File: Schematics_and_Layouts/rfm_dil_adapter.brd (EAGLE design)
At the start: 31.8 x 22.9 mm, 17 parts

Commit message: Added Gerber Files
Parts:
- renumbered CLK to IO5, DCLK to IO1, FSK to IO2, GND1 to AGND, NINT to IO3, NIRQ to IO0, NRES to RES, NSEL to NSS, SDI to MOSI, SDO to MISO
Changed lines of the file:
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@@
 <?xml version="1.0" encoding="utf-8"?>
 <!DOCTYPE eagle SYSTEM "eagle.dtd">
-<eagle version="6.3">
+<eagle version="6.6.0">
 <drawing>
 <settings>
@@
 <setting verticaltext="up"/>
 </settings>
-<grid distance="1.27" unitdist="mm" unit="mm" style="lines" multiple="1" display="yes" altdistance="25" altunitdist="mil" altunit="mil"/>
+<grid distance="1.27" unitdist="mm" unit="mm" style="lines" multiple="1" display="yes" altdistance="12.5" altunitdist="mil" altunit="mil"/>
 <layers>
 <layer number="1" name="Top" color="4" fill="1" visible="yes" active="yes"/>
@@
 </autorouter>
 <elements>
-<element name="U$1" library="fp" package="RFM12_Z" value="RFM12_Z" x="15.24" y="12.7" rot="R270"/>
-<element name="CLK" library="solpad" package="SE13" value="SE13" x="2.54" y="10.16" rot="R270"/>
-<element name="DCLK" library="solpad" package="SE13" value="SE13" x="2.54" y="12.7" rot="R270"/>
-<element name="FSK" library="solpad" package="SE13" value="SE13" x="2.54" y="15.24" rot="R270"/>
-<element name="SDI" library="solpad" package="SE13" value="SE13" x="27.94" y="15.24" rot="R270"/>
-<element name="SDO" library="solpad" package="SE13" value="SE13" x="2.54" y="20.32" rot="R270"/>
-<element name="SCK" library="solpad" package="SE13" value="SE13" x="27.94" y="17.78" rot="R270"/>
-<element name="NSEL" library="solpad" package="SE13" value="SE13" x="27.94" y="20.32" rot="R270"/>
-<element name="GND" library="solpad" package="SE13" value="SE13" x="2.54" y="5.08" rot="R270"/>
-<element name="GND1" library="solpad" package="SE13" value="SE13" x="27.94" y="10.16" rot="R270"/>
-<element name="NRES" library="solpad" package="SE13" value="SE13" x="2.54" y="7.62" rot="R270"/>
-<element name="NIRQ" library="solpad" package="SE13" value="SE13" x="2.54" y="17.78" rot="R270"/>
-<element name="NINT" library="solpad" package="SE13" value="SE13" x="27.94" y="12.7" rot="R270"/>
-<element name="VDD" library="solpad" package="SE13" value="SE13" x="27.94" y="7.62" rot="R270"/>
-<element name="ANT+" library="testpad" package="TP20SQ" value="PTR1TP20SQ" x="22.885" y="2.54">
-<attribute name="TP_SIGNAL_NAME" value="" x="22.885" y="2.54" size="1.778" layer="27" display="off"/>
-</element>
-<element name="ANT_GND" library="testpad" package="TP20SQ" value="PTR1TP20SQ" x="18.635" y="2.54">
-<attribute name="TP_SIGNAL_NAME" value="" x="18.635" y="2.54" size="1.778" layer="27" display="off"/>
-</element>
-<element name="ANT_GND2" library="testpad" package="TP20SQ" value="PTR1TP20SQ" x="27.135" y="2.54">
-<attribute name="TP_SIGNAL_NAME" value="" x="27.135" y="2.54" size="1.778" layer="27" display="off"/>
+<element name="U$1" library="fp" package="RFM12_Z" value="RFM12_Z" x="15.24" y="12.7" smashed="yes" rot="R270"/>
+<element name="IO5" library="solpad" package="SE13" value="SE13" x="2.54" y="10.16" smashed="yes" rot="R270">
+<attribute name="NAME" x="4.191" y="11.43" size="0.8" layer="25" font="vector" ratio="20" rot="R270"/>
+</element>
+<element name="IO1" library="solpad" package="SE13" value="SE13" x="2.54" y="12.7" smashed="yes" rot="R270">
+<attribute name="NAME" x="4.191" y="13.97" size="0.8" layer="25" font="vector" ratio="20" rot="R270"/>
+</element>
+<element name="IO2" library="solpad" package="SE13" value="SE13" x="2.54" y="15.24" smashed="yes" rot="R270">
+<attribute name="NAME" x="4.191" y="16.51" size="0.8" layer="25" font="vector" ratio="20" rot="R270"/>
+</element>
+<element name="MOSI" library="solpad" package="SE13" value="SE13" x="27.94" y="15.24" smashed="yes" rot="R270">
+<attribute name="NAME" x="29.591" y="16.51" size="0.8" layer="25" font="vector" ratio="20" rot="R270"/>
+</element>
+<element name="MISO" library="solpad" package="SE13" value="SE13" x="2.54" y="20.32" smashed="yes" rot="R270">
+<attribute name="NAME" x="4.191" y="21.9075" size="0.8" layer="25" font="vector" ratio="20" rot="R270"/>
+</element>
+<element name="SCK" library="solpad" package="SE13" value="SE13" x="27.94" y="17.78" smashed="yes" rot="R270">
+<attribute name="NAME" x="29.591" y="19.05" size="0.8" layer="25" font="vector" ratio="20" rot="R270"/>
+</element>
+<element name="NSS" library="solpad" package="SE13" value="SE13" x="27.94" y="20.32" smashed="yes" rot="R270">
+<attribute name="NAME" x="29.591" y="21.59" size="0.8" layer="25" font="vector" ratio="20" rot="R270"/>
+</element>
+<element name="GND" library="solpad" package="SE13" value="SE13" x="2.54" y="5.08" smashed="yes" rot="R270">
+<attribute name="NAME" x="5.0165" y="3.81" size="0.8" layer="25" font="vector" ratio="20" rot="R90"/>
+</element>
+<element name="AGND" library="solpad" package="SE13" value="SE13" x="27.94" y="10.16" smashed="yes" rot="R270">
+<attribute name="NAME" x="29.591" y="11.7475" size="0.8" layer="25" font="vector" ratio="20" rot="R270"/>
+</element>
+<element name="RES" library="solpad" package="SE13" value="SE13" x="2.54" y="7.62" smashed="yes" rot="R270">
+<attribute name="NAME" x="4.191" y="8.89" size="0.8" layer="25" font="vector" ratio="20" rot="R270"/>
+</element>
+<element name="IO0" library="solpad" package="SE13" value="SE13" x="2.54" y="17.78" smashed="yes" rot="R270">
+<attribute name="NAME" x="4.191" y="19.05" size="0.8" layer="25" font="vector" ratio="20" rot="R270"/>
+</element>
+<element name="IO3" library="solpad" package="SE13" value="SE13" x="27.94" y="12.7" smashed="yes" rot="R270">
+<attribute name="NAME" x="29.591" y="13.6525" size="0.8" layer="25" font="vector" ratio="20" rot="R270"/>
+</element>
+<element name="VDD" library="solpad" package="SE13" value="SE13" x="27.94" y="7.62" smashed="yes" rot="R270">
+<attribute name="NAME" x="29.591" y="8.5725" size="0.8" layer="25" font="vector" ratio="20" rot="R270"/>
+</element>
+<element name="ANT+" library="testpad" package="TP20SQ" value="PTR1TP20SQ" x="22.885" y="2.54" smashed="yes">
+<attribute name="TP_SIGNAL_NAME" value="" x="22.885" y="0" size="1" layer="37"/>
+</element>
+<element name="ANT_GND" library="testpad" package="TP20SQ" value="PTR1TP20SQ" x="18.635" y="2.54" smashed="yes">
+<attribute name="TP_SIGNAL_NAME" value="" x="18.635" y="0" size="1" layer="37"/>
+</element>
+<element name="ANT_GND2" library="testpad" package="TP20SQ" value="PTR1TP20SQ" x="27.135" y="2.54" smashed="yes">
+<attribute name="TP_SIGNAL_NAME" value="" x="27.135" y="0" size="1" layer="37"/>
 </element>
 </elements>
@@
 <signal name="N$1">
 <contactref element="U$1" pad="CLK"/>
-<contactref element="CLK" pad="MP"/>
+<contactref element="IO5" pad="MP"/>
 <wire x1="2.54" y1="10.16" x2="3.08" y2="10.7" width="0.8128" layer="1"/>
 <wire x1="3.08" y1="10.7" x2="7.24" y2="10.7" width="0.8128" layer="1"/>
@@
 <signal name="N$2">
 <contactref element="U$1" pad="DCLK"/>
-<contactref element="DCLK" pad="MP"/>
+<contactref element="IO1" pad="MP"/>
 <wire x1="2.54" y1="12.7" x2="7.24" y2="12.7" width="0.8128" layer="1"/>
 </signal>
 <signal name="N$3">
 <contactref element="U$1" pad="FSK"/>
-<contactref element="FSK" pad="MP"/>
+<contactref element="IO2" pad="MP"/>
 <wire x1="2.54" y1="15.24" x2="3.08" y2="14.7" width="0.8128" layer="1"/>
 <wire x1="3.08" y1="14.7" x2="7.24" y2="14.7" width="0.8128" layer="1"/>
@@
 <signal name="N$4">
 <contactref element="U$1" pad="SDI"/>
-<contactref element="SDI" pad="MP"/>
+<contactref element="MOSI" pad="MP"/>
 <wire x1="27.94" y1="15.24" x2="27.4" y2="14.7" width="0.8128" layer="1"/>
 <wire x1="27.4" y1="14.7" x2="23.240003125" y2="14.7" width="0.8128" layer="1"/>
@@
 <signal name="N$5">
 <contactref element="U$1" pad="SDO"/>
-<contactref element="SDO" pad="MP"/>
+<contactref element="MISO" pad="MP"/>
 <wire x1="2.54" y1="20.32" x2="5.62" y2="20.32" width="0.8128" layer="1"/>
 <wire x1="5.62" y1="20.32" x2="7.239996875" y2="18.700003125" width="0.8128" layer="1"/>
@@
 <signal name="N$7">
 <contactref element="U$1" pad="NSEL"/>
-<contactref element="NSEL" pad="MP"/>
+<contactref element="NSS" pad="MP"/>
 <wire x1="27.94" y1="20.32" x2="24.86" y2="20.32" width="0.8128" layer="1"/>
 <wire x1="24.86" y1="20.32" x2="23.24" y2="18.7" width="0.8128" layer="1"/>
@@
 <signal name="N$11">
 <contactref element="U$1" pad="NRES"/>
-<contactref element="NRES" pad="MP"/>
+<contactref element="RES" pad="MP"/>
 <wire x1="2.54" y1="7.62" x2="4.159996875" y2="7.62" width="0.8128" layer="1"/>
 <wire x1="4.159996875" y1="7.62" x2="5.23999375" y2="8.699996875" width="0.8128" layer="1"/>
@@
 <signal name="N$12">
 <contactref element="U$1" pad="NIRQ"/>
-<contactref element="NIRQ" pad="MP"/>
+<contactref element="IO0" pad="MP"/>
 <wire x1="2.54" y1="17.78" x2="4.159996875" y2="17.78" width="0.8128" layer="1"/>
 <wire x1="4.159996875" y1="17.78" x2="5.23999375" y2="16.700003125" width="0.8128" layer="1"/>
@@
 <signal name="N$13">
 <contactref element="U$1" pad="NINT"/>
-<contactref element="NINT" pad="MP"/>
+<contactref element="IO3" pad="MP"/>
 <wire x1="27.94" y1="12.7" x2="23.24" y2="12.7" width="0.8128" layer="1"/>
 </signal>
@@
 <wire x1="5.62" y1="5.08" x2="7.24" y2="6.7" width="0.8128" layer="1"/>
 <contactref element="U$1" pad="GND1"/>
-<contactref element="GND1" pad="MP"/>
+<contactref element="AGND" pad="MP"/>
 <wire x1="27.94" y1="10.16" x2="27.4" y2="10.7" width="0.8128" layer="1"/>
 <wire x1="27.4" y1="10.7" x2="23.24" y2="10.7" width="0.8128" layer="1"/>

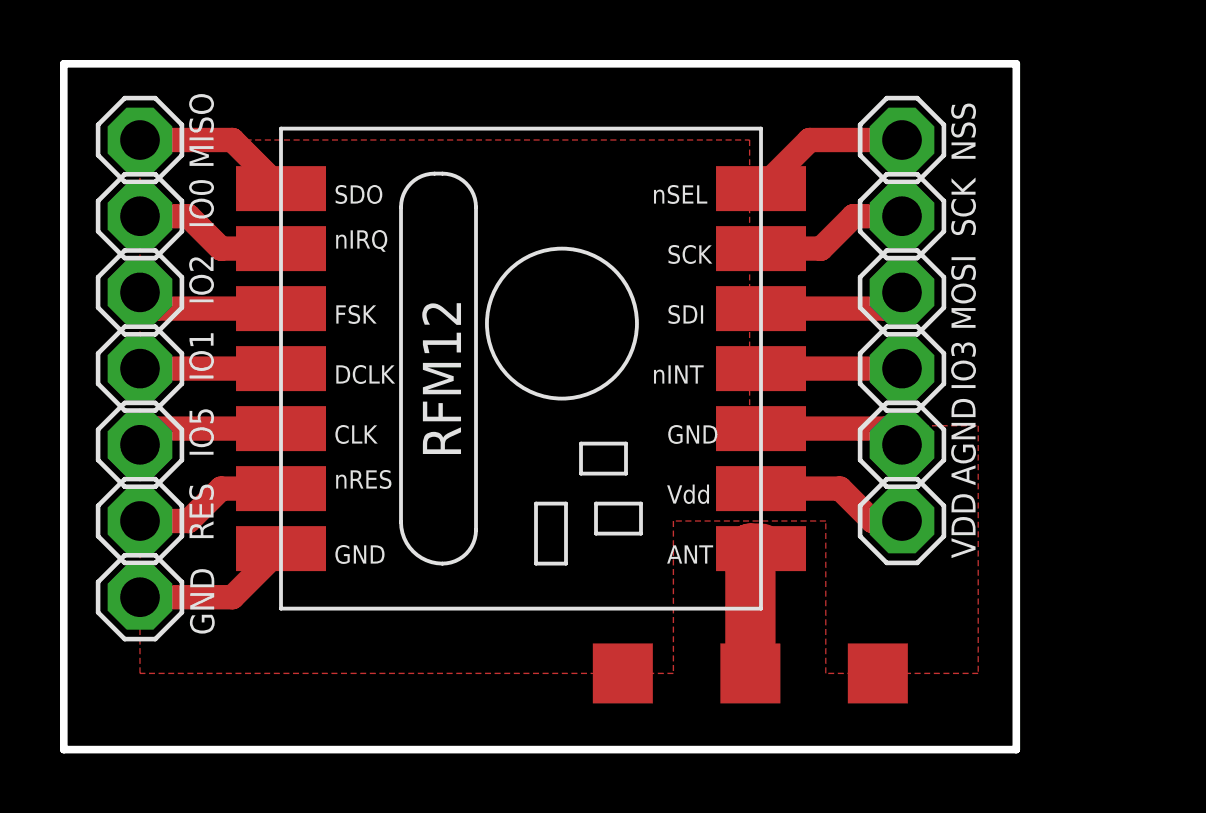
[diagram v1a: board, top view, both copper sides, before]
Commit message: Angleichung von Handbuch und Layouts
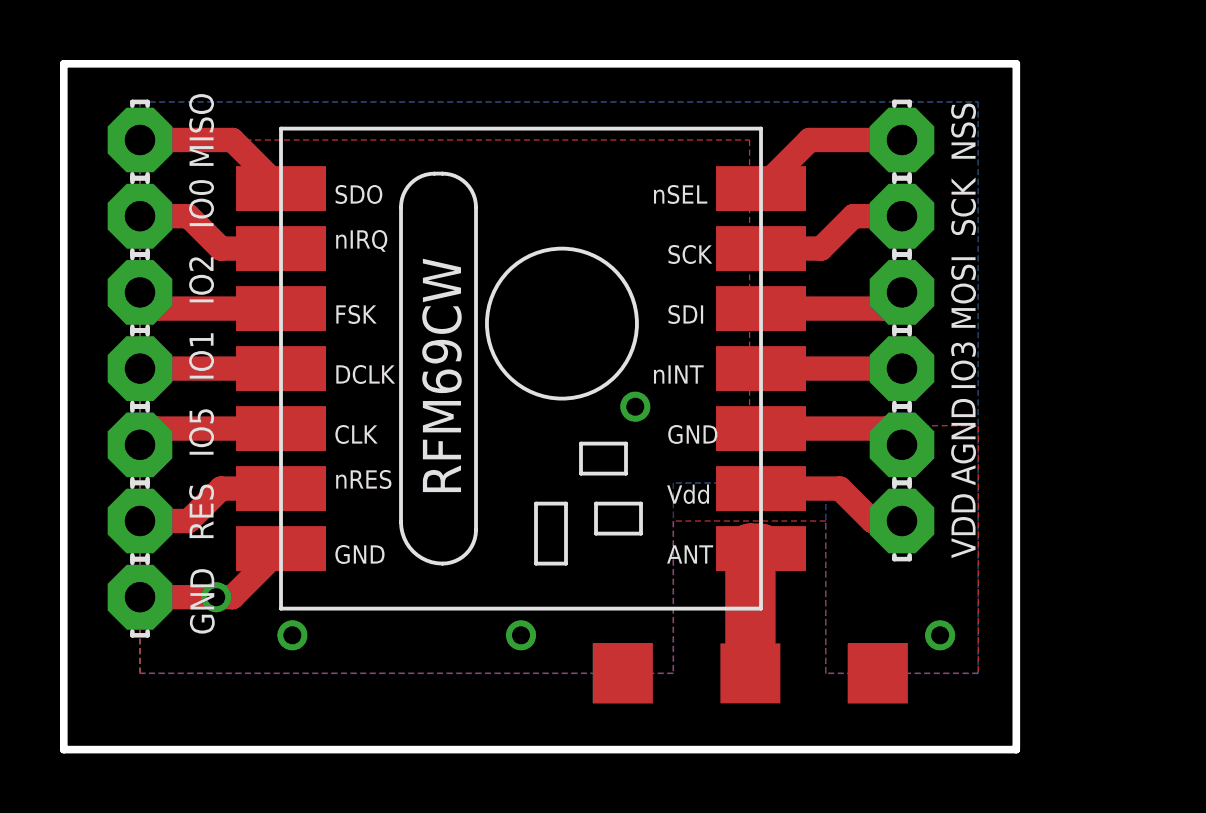
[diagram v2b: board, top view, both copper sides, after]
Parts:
- added ANT_GND1, ANT_GND3: PTR1TP20SQ, testpad:TP20SQ
- AGND, GND, IO0, IO1, IO2, IO3, IO5, MISO, MOSI, NSS, RES, SCK, VDD: value SE13 -> LSP10; device solpad:SE13 -> solpad:LSP10
- U$1: value RFM12_Z -> RFM12_ZSMD
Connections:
- net GND: now also ANT_GND1.TP, ANT_GND3.TP
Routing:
- net GND: vias 0 -> 5
- added copper zone on layer 16, net GND
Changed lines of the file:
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@@
 <setting verticaltext="up"/>
 </settings>
-<grid distance="1.27" unitdist="mm" unit="mm" style="lines" multiple="1" display="yes" altdistance="12.5" altunitdist="mil" altunit="mil"/>
+<grid distance="1.27" unitdist="mm" unit="mm" style="lines" multiple="1" display="yes" altdistance="12.5" altunitdist="mil" altunit="mm"/>
 <layers>
 <layer number="1" name="Top" color="4" fill="1" visible="yes" active="yes"/>
@@
 <layer number="97" name="Info" color="7" fill="1" visible="no" active="no"/>
 <layer number="98" name="Guide" color="6" fill="1" visible="no" active="no"/>
-<layer number="116" name="centerDrill" color="7" fill="1" visible="yes" active="yes"/>
+<layer number="116" name="centerDrill" color="7" fill="1" visible="no" active="yes"/>
 </layers>
 <board>
@@
 <wire x1="31.75" y1="0" x2="31.75" y2="22.86" width="0.254" layer="20"/>
 <wire x1="31.75" y1="22.86" x2="0" y2="22.86" width="0.254" layer="20"/>
-<circle x="2.54" y="10.16" radius="0.605" width="0.81" layer="116"/>
-<circle x="2.54" y="12.7" radius="0.605" width="0.81" layer="116"/>
-<circle x="2.54" y="15.24" radius="0.605" width="0.81" layer="116"/>
-<circle x="2.54" y="5.08" radius="0.605" width="0.81" layer="116"/>
-<circle x="27.94" y="10.16" radius="0.605" width="0.81" layer="116"/>
-<circle x="27.94" y="12.7" radius="0.605" width="0.81" layer="116"/>
-<circle x="2.54" y="17.78" radius="0.605" width="0.81" layer="116"/>
-<circle x="2.54" y="7.62" radius="0.605" width="0.81" layer="116"/>
-<circle x="27.94" y="20.32" radius="0.605" width="0.81" layer="116"/>
-<circle x="27.94" y="17.78" radius="0.605" width="0.81" layer="116"/>
-<circle x="27.94" y="15.24" radius="0.605" width="0.81" layer="116"/>
-<circle x="2.54" y="20.32" radius="0.605" width="0.81" layer="116"/>
-<circle x="27.94" y="7.62" radius="0.605" width="0.81" layer="116"/>
 </plain>
 <attributes>
@@
 </autorouter>
 <elements>
-<element name="U$1" library="fp" package="RFM12_Z" value="RFM12_Z" x="15.24" y="12.7" smashed="yes" rot="R270"/>
-<element name="IO5" library="solpad" package="SE13" value="SE13" x="2.54" y="10.16" smashed="yes" rot="R270">
+<element name="U$1" library="fp" package="RFM12_Z" value="RFM12_ZSMD" x="15.24" y="12.7" smashed="yes" rot="R270"/>
+<element name="IO5" library="solpad" package="LSP10" value="LSP10" x="2.54" y="10.16" smashed="yes" rot="R270">
 <attribute name="NAME" x="4.191" y="11.43" size="0.8" layer="25" font="vector" ratio="20" rot="R270"/>
 </element>
-<element name="IO1" library="solpad" package="SE13" value="SE13" x="2.54" y="12.7" smashed="yes" rot="R270">
+<element name="IO1" library="solpad" package="LSP10" value="LSP10" x="2.54" y="12.7" smashed="yes" rot="R270">
 <attribute name="NAME" x="4.191" y="13.97" size="0.8" layer="25" font="vector" ratio="20" rot="R270"/>
 </element>
-<element name="IO2" library="solpad" package="SE13" value="SE13" x="2.54" y="15.24" smashed="yes" rot="R270">
+<element name="IO2" library="solpad" package="LSP10" value="LSP10" x="2.54" y="15.24" smashed="yes" rot="R270">
 <attribute name="NAME" x="4.191" y="16.51" size="0.8" layer="25" font="vector" ratio="20" rot="R270"/>
 </element>
-<element name="MOSI" library="solpad" package="SE13" value="SE13" x="27.94" y="15.24" smashed="yes" rot="R270">
+<element name="MOSI" library="solpad" package="LSP10" value="LSP10" x="27.94" y="15.24" smashed="yes" rot="R270">
 <attribute name="NAME" x="29.591" y="16.51" size="0.8" layer="25" font="vector" ratio="20" rot="R270"/>
 </element>
-<element name="MISO" library="solpad" package="SE13" value="SE13" x="2.54" y="20.32" smashed="yes" rot="R270">
+<element name="MISO" library="solpad" package="LSP10" value="LSP10" x="2.54" y="20.32" smashed="yes" rot="R270">
 <attribute name="NAME" x="4.191" y="21.9075" size="0.8" layer="25" font="vector" ratio="20" rot="R270"/>
 </element>
-<element name="SCK" library="solpad" package="SE13" value="SE13" x="27.94" y="17.78" smashed="yes" rot="R270">
+<element name="SCK" library="solpad" package="LSP10" value="LSP10" x="27.94" y="17.78" smashed="yes" rot="R270">
 <attribute name="NAME" x="29.591" y="19.05" size="0.8" layer="25" font="vector" ratio="20" rot="R270"/>
 </element>
-<element name="NSS" library="solpad" package="SE13" value="SE13" x="27.94" y="20.32" smashed="yes" rot="R270">
+<element name="NSS" library="solpad" package="LSP10" value="LSP10" x="27.94" y="20.32" smashed="yes" rot="R270">
 <attribute name="NAME" x="29.591" y="21.59" size="0.8" layer="25" font="vector" ratio="20" rot="R270"/>
 </element>
-<element name="GND" library="solpad" package="SE13" value="SE13" x="2.54" y="5.08" smashed="yes" rot="R270">
+<element name="GND" library="solpad" package="LSP10" value="LSP10" x="2.54" y="5.08" smashed="yes" rot="R270">
 <attribute name="NAME" x="5.0165" y="3.81" size="0.8" layer="25" font="vector" ratio="20" rot="R90"/>
 </element>
-<element name="AGND" library="solpad" package="SE13" value="SE13" x="27.94" y="10.16" smashed="yes" rot="R270">
+<element name="AGND" library="solpad" package="LSP10" value="LSP10" x="27.94" y="10.16" smashed="yes" rot="R270">
 <attribute name="NAME" x="29.591" y="11.7475" size="0.8" layer="25" font="vector" ratio="20" rot="R270"/>
 </element>
-<element name="RES" library="solpad" package="SE13" value="SE13" x="2.54" y="7.62" smashed="yes" rot="R270">
+<element name="RES" library="solpad" package="LSP10" value="LSP10" x="2.54" y="7.62" smashed="yes" rot="R270">
 <attribute name="NAME" x="4.191" y="8.89" size="0.8" layer="25" font="vector" ratio="20" rot="R270"/>
 </element>
-<element name="IO0" library="solpad" package="SE13" value="SE13" x="2.54" y="17.78" smashed="yes" rot="R270">
+<element name="IO0" library="solpad" package="LSP10" value="LSP10" x="2.54" y="17.78" smashed="yes" rot="R270">
 <attribute name="NAME" x="4.191" y="19.05" size="0.8" layer="25" font="vector" ratio="20" rot="R270"/>
 </element>
-<element name="IO3" library="solpad" package="SE13" value="SE13" x="27.94" y="12.7" smashed="yes" rot="R270">
+<element name="IO3" library="solpad" package="LSP10" value="LSP10" x="27.94" y="12.7" smashed="yes" rot="R270">
 <attribute name="NAME" x="29.591" y="13.6525" size="0.8" layer="25" font="vector" ratio="20" rot="R270"/>
 </element>
-<element name="VDD" library="solpad" package="SE13" value="SE13" x="27.94" y="7.62" smashed="yes" rot="R270">
+<element name="VDD" library="solpad" package="LSP10" value="LSP10" x="27.94" y="7.62" smashed="yes" rot="R270">
 <attribute name="NAME" x="29.591" y="8.5725" size="0.8" layer="25" font="vector" ratio="20" rot="R270"/>
 </element>
@@
 <element name="ANT_GND2" library="testpad" package="TP20SQ" value="PTR1TP20SQ" x="27.135" y="2.54" smashed="yes">
 <attribute name="TP_SIGNAL_NAME" value="" x="27.135" y="0" size="1" layer="37"/>
+</element>
+<element name="ANT_GND1" library="testpad" package="TP20SQ" value="PTR1TP20SQ" x="18.635" y="2.54" smashed="yes" rot="MR0">
+<attribute name="TP_SIGNAL_NAME" value="" x="18.635" y="0" size="1" layer="38" rot="MR0"/>
+</element>
+<element name="ANT_GND3" library="testpad" package="TP20SQ" value="PTR1TP20SQ" x="27.135" y="2.54" smashed="yes" rot="MR0">
+<attribute name="TP_SIGNAL_NAME" value="" x="27.135" y="0" size="1" layer="38" rot="MR0"/>
 </element>
 </elements>
@@
 <wire x1="27.4" y1="10.7" x2="23.24" y2="10.7" width="0.8128" layer="1"/>
 <contactref element="ANT_GND2" pad="TP"/>
+<polygon width="0.4064" layer="16">
+<vertex x="2.54" y="2.54"/>
+<vertex x="2.54" y="21.59"/>
+<vertex x="30.48" y="21.59"/>
+<vertex x="30.48" y="2.54"/>
+<vertex x="25.4" y="2.54"/>
+<vertex x="25.4" y="8.89"/>
+<vertex x="20.32" y="8.89"/>
+<vertex x="20.32" y="2.54"/>
+</polygon>
+<via x="7.62" y="3.81" extent="1-16" drill="0.6" shape="square"/>
+<via x="15.24" y="3.81" extent="1-16" drill="0.6" shape="square"/>
+<via x="29.21" y="3.81" extent="1-16" drill="0.6" shape="square"/>
+<via x="5.08" y="5.08" extent="1-16" drill="0.6" shape="square"/>
+<via x="19.05" y="11.43" extent="1-16" drill="0.6" shape="square"/>
+<contactref element="ANT_GND3" pad="TP"/>
+<contactref element="ANT_GND1" pad="TP"/>
 </signal>
 </signals>
